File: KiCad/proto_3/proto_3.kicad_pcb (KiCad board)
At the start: 2 copper layers, 129 x 49 mm, 13 parts, among them J1 1729128, J2 1729128

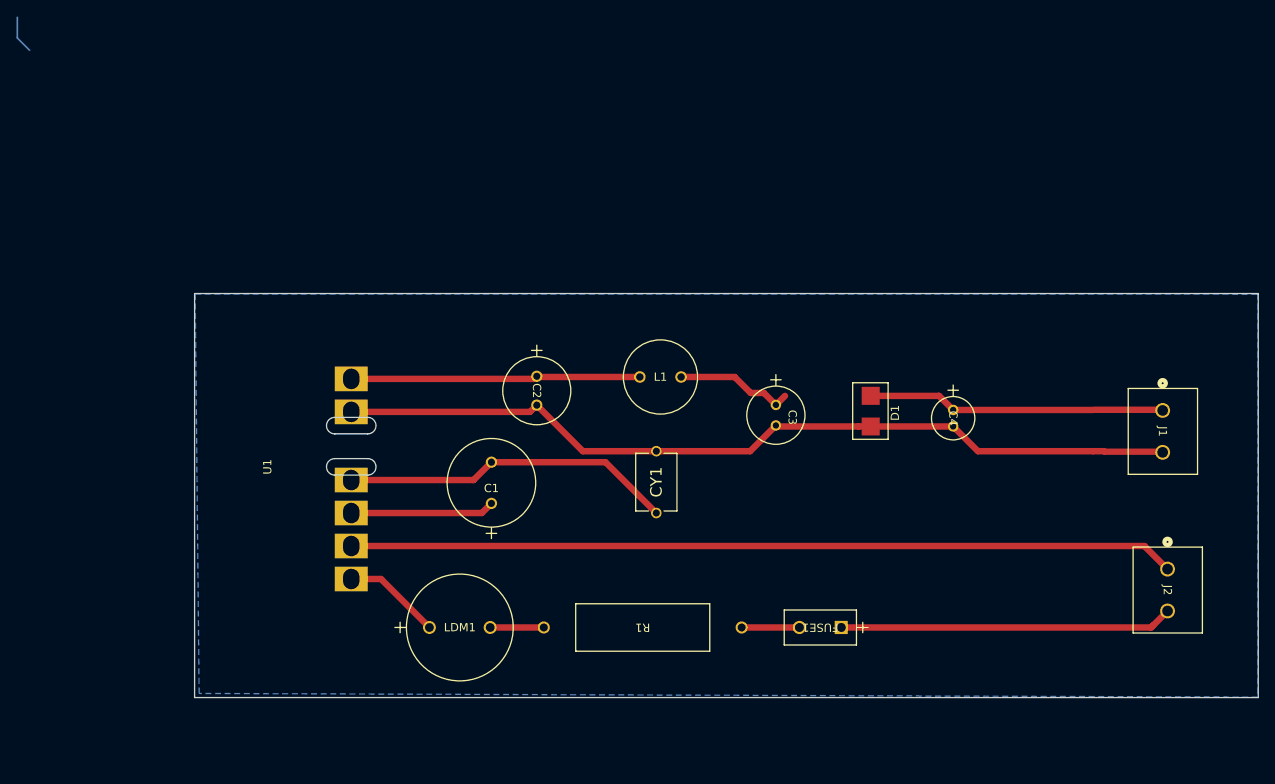
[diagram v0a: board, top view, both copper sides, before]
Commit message: changed space between traces on high voltage rail
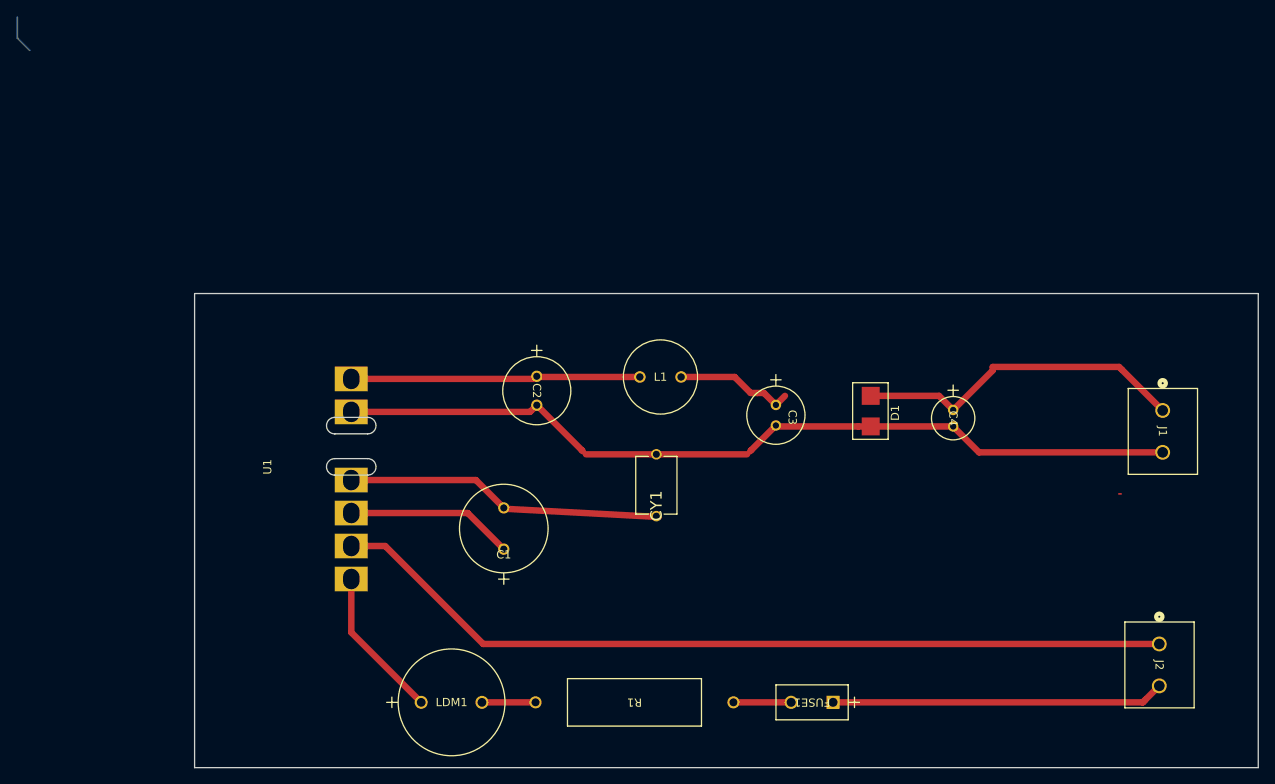
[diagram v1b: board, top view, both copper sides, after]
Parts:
- moved FUSE1 9.13 mm to (174.9, 137.6)
- moved LDM1 9.13 mm to (125.0, 137.6)
- moved R1 9.13 mm to (162.8, 137.6)
- moved J2 9.13 mm to (214.5, 130.5)
- moved C1 5.75 mm to (135.0, 119.0)
- moved CY1 0.38 mm to (153.5, 111.2)
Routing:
- net /ACDC_VCAP_NEG: track 40.5 -> 19.9 mm
- net /AC_FILTER_OUT: track 11.9 -> 18.5 mm
- net /DC_OUT: track 52.2 -> 57.2 mm
- net /ACDC_VCAP_POS: track 17.5 -> 20.3 mm
- net /AC_IN_NEUTRAL: track 100.2 -> 102.9 mm
- net /GND: track 103.5 -> 104.6 mm
- removed copper zone on B.Cu, net /GND
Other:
- board size 129 x 49 mm -> 129 x 57.5 mm
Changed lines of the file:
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@@
 	(footprint "Resistor-300-3A:res2_1-1625892-1_TEC"
 		(layer "F.Cu")
-		(at 163.849749 128.5 180)
+		(at 162.849749 137.58 180)
 		(tags "ROX3SJ12R ")
 		(property "Reference" "R1"
@@
 	(footprint "stuff:AIUR-06_ABR"
 		(layer "F.Cu")
-		(at 125.98375 128.5)
+		(at 124.98375 137.58)
 		(tags "AIUR-06-472K ")
 		(property "Reference" "LDM1"
@@
 	(footprint "Capacitor-10uF-450V:CAP_BX_10x20_RUB"
 		(layer "F.Cu")
-		(at 133.5 113.45325 90)
+		(at 135 119 90)
 		(tags "450BXC10MEFC10X20 ")
 		(property "Reference" "C1"
-			(at 1.83325 0 0)
+			(at -0.66675 0 0)
 			(unlocked yes)
 			(layer "F.SilkS")
@@
 		)
 		(fp_text user "${REFERENCE}"
-			(at 1.83325 0 0)
+			(at -0.66675 0 0)
 			(unlocked yes)
 			(layer "F.Fab")
@@
 	(footprint "Capacitor-1nF-400V:CAP_DE2E3SA102MN3AY02F"
 		(layer "F.Cu")
-		(at 153.5 110.87 90)
+		(at 153.5 111.25 90)
 		(property "Reference" "CY1"
-			(at 0 0 90)
+			(at -2.5 0 90)
 			(layer "F.SilkS")
 			(effects
@@
 	(footprint "fuse_300V_1a:FUSE_36911_LTF"
 		(layer "F.Cu")
-		(at 175.92975 128.5 180)
+		(at 174.92975 137.58 180)
 		(tags "36911000000 ")
 		(property "Reference" "FUSE1"
@@
 	(footprint "stuff:CONN_1729128_PXC"
 		(layer "F.Cu")
-		(at 215.5 121.42 -90)
+		(at 214.5 130.5 -90)
 		(tags "1729128 ")
 		(property "Reference" "J2"
@@
 		(embedded_fonts no)
 	)
+	(gr_line
+		(start 135.1 114.1)
+		(end 153.8 115.1)
+		(stroke
+			(width 0.7814)
+			(type solid)
+		)
+		(layer "F.Cu")
+		(net 2)
+	)
 	(gr_rect
 		(start 97.5 88)
-		(end 226.5 137)
+		(end 226.5 145.5)
 		(stroke
 			(width 0.05)
@@
 	)
 	(segment
-		(start 132.33325 114.62)
-		(end 116.5 114.62)
+		(start 116.5 114.62)
+		(end 130.62 114.62)
 		(width 0.7814)
 		(layer "F.Cu")
@@
 	)
 	(segment
-		(start 133.5 113.45325)
-		(end 132.33325 114.62)
+		(start 130.62 114.62)
+		(end 135 119)
 		(width 0.7814)
 		(layer "F.Cu")
@@
 	)
 	(segment
-		(start 147.33325 108.45325)
-		(end 153.5 114.62)
+		(start 131.62 110.62)
+		(end 135 114)
 		(width 0.7814)
 		(layer "F.Cu")
@@
 	)
 	(segment
-		(start 133.5 108.45325)
-		(end 147.33325 108.45325)
+		(start 116.5 110.62)
+		(end 131.62 110.62)
 		(width 0.7814)
 		(layer "F.Cu")
@@
 	)
 	(segment
-		(start 133.5 108.45325)
-		(end 131.33325 110.62)
-		(width 0.7814)
-		(layer "F.Cu")
-		(net 2)
-	)
-	(segment
-		(start 131.33325 110.62)
-		(end 116.5 110.62)
-		(width 0.7814)
-		(layer "F.Cu")
-		(net 2)
-	)
-	(segment
-		(start 192.5 107.12)
-		(end 206.5 107.12)
+		(start 192.64 107.26)
+		(end 214.9092 107.26)
+		(width 0.7814)
+		(layer "F.Cu")
+		(net 3)
+	)
+	(segment
+		(start 144.463249 107)
+		(end 144.583249 107.12)
+		(width 0.7814)
+		(layer "F.Cu")
+		(net 3)
+	)
+	(segment
+		(start 189.5 104.12)
+		(end 192.64 107.26)
+		(width 0.7814)
+		(layer "F.Cu")
+		(net 3)
+	)
+	(segment
+		(start 153.5 107.5)
+		(end 164.5 107.5)
 		(width 0.7814)
 		(layer "F.Cu")
@@
 	)
 	(segment
+		(start 164.88 107.12)
+		(end 165 107)
+		(width 0.7814)
+		(layer "F.Cu")
+		(net 3)
+	)
+	(segment
 		(start 138.184751 102.352)
 		(end 139 101.536751)
@@
 	)
 	(segment
-		(start 139 101.536751)
-		(end 144.583249 107.12)
-		(width 0.7814)
+		(start 144.963249 107.5)
+		(end 144.463249 107)
+		(width 0.2)
 		(layer "F.Cu")
 		(net 3)
 	)
 	(segment
-		(start 153.5 107.12)
-		(end 164.88 107.12)
+		(start 153.5 107.5)
+		(end 144.963249 107.5)
 		(width 0.7814)
 		(layer "F.Cu")
@@
 	)
 	(segment
-		(start 206.5 107.12)
-		(end 207.8 107.12)
-		(width 0.7814)
+		(start 209.8692 112.3)
+		(end 209.6 112.3)
+		(width 0.2)
 		(layer "F.Cu")
 		(net 3)
 	)
 	(segment
-		(start 164.88 107.12)
+		(start 165 107)
 		(end 168 104)
 		(width 0.7814)
@@
 	)
 	(segment
-		(start 144.583249 107.12)
-		(end 153.5 107.12)
-		(width 0.7814)
-		(layer "F.Cu")
-		(net 3)
-	)
-	(segment
-		(start 207.860799 107.18)
-		(end 214.9092 107.18)
-		(width 0.7814)
-		(layer "F.Cu")
-		(net 3)
-	)
-	(segment
-		(start 189.5 104.12)
-		(end 192.5 107.12)
-		(width 0.7814)
+		(start 164.5 107.5)
+		(end 165 107)
+		(width 0.2)
 		(layer "F.Cu")
 		(net 3)
@@
 		(start 116.5 102.352)
 		(end 138.184751 102.352)
+		(width 0.7814)
+		(layer "F.Cu")
+		(net 3)
+	)
+	(segment
+		(start 139 101.536751)
+		(end 144.463249 107)
 		(width 0.7814)
 		(layer "F.Cu")
@@
 	)
 	(segment
+		(start 209.9646 97.2354)
+		(end 209.8 97.0708)
+		(width 0.2)
+		(layer "F.Cu")
+		(net 5)
+	)
+	(segment
 		(start 167.1092 100.62)
 		(end 168 101.5108)
@@
 	)
 	(segment
-		(start 206.640799 102.1)
-		(end 214.9092 102.1)
+		(start 194.3 96.9)
+		(end 209.6292 96.9)
+		(width 0.7814)
+		(layer "F.Cu")
+		(net 5)
+	)
+	(segment
+		(start 209.6292 96.9)
+		(end 209.9646 97.2354)
+		(width 0.7814)
+		(layer "F.Cu")
+		(net 5)
+	)
+	(segment
+		(start 189.5 102.12)
+		(end 194.3 97.32)
+		(width 0.7814)
+		(layer "F.Cu")
+		(net 5)
+	)
+	(segment
+		(start 209.9646 97.2354)
+		(end 214.9092 102.18)
 		(width 0.7814)
 		(layer "F.Cu")
@@
 	)
 	(segment
+		(start 194.3 97.32)
+		(end 194.3 96.9)
+		(width 0.7814)
+		(layer "F.Cu")
+		(net 5)
+	)
+	(segment
 		(start 187.79 100.41)
 		(end 179.5 100.41)
@@
 	)
 	(segment
-		(start 189.5 102.12)
-		(end 206.5 102.12)
-		(width 0.7814)
-		(layer "F.Cu")
-		(net 5)
-	)
-	(segment
 		(start 164.94 100.06)
 		(end 166.5492 100.06)
@@
 	)
 	(segment
-		(start 163.849751 128.5)
-		(end 170.84975 128.5)
+		(start 162.849751 137.58)
+		(end 169.84975 137.58)
 		(width 0.7814)
 		(layer "F.Cu")
@@
 	)
 	(segment
-		(start 213.5 128.5)
-		(end 215.5 126.5)
+		(start 212.5 137.58)
+		(end 214.5 135.58)
 		(width 0.7814)
 		(layer "F.Cu")
@@
 	)
 	(segment
-		(start 175.92975 128.5)
-		(end 213.5 128.5)
+		(start 174.92975 137.58)
+		(end 212.5 137.58)
 		(width 0.7814)
 		(layer "F.Cu")
@@
 	)
 	(segment
-		(start 213.5 128.5)
-		(end 213.8 128.2)
+		(start 212.5 137.58)
+		(end 212.8 137.28)
 		(width 0.7814)
 		(layer "F.Cu")
@@
 	)
 	(segment
-		(start 212.7 118.62)
-		(end 215.5 121.42)
+		(start 132.5 130.5)
+		(end 214.5 130.5)
 		(width 0.7814)
 		(layer "F.Cu")
@@
 	(segment
 		(start 116.5 118.62)
-		(end 212.7 118.62)
+		(end 120.62 118.62)
 		(width 0.7814)
 		(layer "F.Cu")
@@
 	)
 	(segment
-		(start 139.84975 128.5)
-		(end 133.34975 128.5)
+		(start 120.62 118.62)
+		(end 132.5 130.5)
+		(width 0.7814)
+		(layer "F.Cu")
+		(net 8)
+	)
+	(segment
+		(start 138.84975 137.58)
+		(end 132.34975 137.58)
 		(width 0.7814)
 		(layer "F.Cu")
@@
 	)
 	(segment
-		(start 120.10375 122.62)
-		(end 125.98375 128.5)
+		(start 116.5 122.62)
+		(end 116.5 129.09625)
 		(width 0.7814)
 		(layer "F.Cu")
@@
 	)
 	(segment
-		(start 116.5 122.62)
-		(end 120.10375 122.62)
+		(start 116.5 129.09625)
+		(end 124.98375 137.58)
 		(width 0.7814)
 		(layer "F.Cu")
 		(net 10)
 	)
-	(zone
-		(net 3)
-		(net_name "/GND")
-		(layer "B.Cu")
-		(hatch edge 0.5)
-		(connect_pads
-			(clearance 0.5)
-		)
-		(min_thickness 0.25)
-		(filled_areas_thickness no)
-		(fill yes
-			(thermal_gap 0.5)
-			(thermal_bridge_width 0.5)
-		)
-		(polygon
-			(pts
-				(xy 97.575 88.05) (xy 226.425 88.075) (xy 226.45 136.95) (xy 98.05 136.5)
-			)
-		)
-	)
 	(embedded_fonts no)

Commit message: added step files back to footprints, moved traces around
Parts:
- moved CY1 0.35 mm to (153.6, 110.9)
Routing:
- net /DC_OUT: track 57.2 -> 64.2 mm
- net /GND: track 104.6 -> 105.1 mm
- net /AC_IN_NEUTRAL: track 102.9 -> 103.4 mm
- added copper zone on B.Cu, net /GND
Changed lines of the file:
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@@
 		)
 		(embedded_fonts no)
+		(model "/home/none/Downloads/3d_models/UFW1C471MPD(1)/CAP_RHT_8X11P5_NCH.step"
+			(offset
+				(xyz 0 0 0)
+			)
+			(scale
+				(xyz 1 1 1)
+			)
+			(rotate
+				(xyz 0 0 0)
+			)
+		)
 	)
 	(footprint "stuff:IND_RLB9012-4R7ML"
@@
 		(embedded_fonts no)
 		(model "/home/none/Downloads/3d_models/UFW1H0R1MDD1TA(1)/CAP_UEP_5X11_NCH.step"
-			(hide yes)
 			(offset
 				(xyz 0 0 0)
@@
 	(footprint "Capacitor-1nF-400V:CAP_DE2E3SA102MN3AY02F"
 		(layer "F.Cu")
-		(at 153.5 111.25 90)
+		(at 153.55 110.9 90)
 		(property "Reference" "CY1"
-			(at -2.5 0 90)
+			(at 0 0 90)
 			(layer "F.SilkS")
 			(effects
@@
 		(embedded_fonts no)
 		(model "/home/none/Downloads/3d_models/35ZLJ100M6_3X11(1)/CAP_6_3X11_RUB.step"
-			(hide yes)
 			(offset
 				(xyz 0 0 0)
@@
 	)
 	(gr_line
-		(start 135.1 114.1)
-		(end 153.8 115.1)
+		(start 135 114)
+		(end 137 114.5)
+		(stroke
+			(width 0.7814)
+			(type solid)
+		)
+		(layer "F.Cu")
+		(net 2)
+	)
+	(gr_line
+		(start 137 114.5)
+		(end 153.55 114.65)
 		(stroke
 			(width 0.7814)
@@
 	)
 	(segment
-		(start 192.64 107.26)
-		(end 214.9092 107.26)
+		(start 189.6 104.1)
+		(end 189.9354 104.1)
 		(width 0.7814)
 		(layer "F.Cu")
@@
 	)
 	(segment
-		(start 189.5 104.12)
-		(end 192.64 107.26)
+		(start 153.5 107.2)
+		(end 164.5 107.2)
 		(width 0.7814)
 		(layer "F.Cu")
@@
 	)
 	(segment
-		(start 153.5 107.5)
-		(end 164.5 107.5)
+		(start 168 104.12)
+		(end 178 104.12)
 		(width 0.7814)
 		(layer "F.Cu")
@@
 	)
 	(segment
-		(start 168 104.12)
-		(end 178 104.12)
+		(start 193 107.5)
+		(end 214.6692 107.5)
 		(width 0.7814)
 		(layer "F.Cu")
@@
 	)
 	(segment
-		(start 153.5 107.5)
-		(end 144.963249 107.5)
+		(start 153.468375 107.2)
+		(end 144.931624 107.2)
 		(width 0.7814)
 		(layer "F.Cu")
@@
 	)
 	(segment
+		(start 189.5277 104.0277)
+		(end 193 107.5)
+		(width 0.7814)
+		(layer "F.Cu")
+		(net 3)
+	)
+	(segment
+		(start 214.6692 107.5)
+		(end 214.9092 107.26)
+		(width 0.7814)
+		(layer "F.Cu")
+		(net 3)
+	)
+	(segment
 		(start 116.5 102.352)
 		(end 138.184751 102.352)
@@
 	)
 	(segment
-		(start 156.5 98.12)
-		(end 163 98.12)
+		(start 189.5154 102.18)
+		(end 203.5 102.18)
 		(width 0.7814)
 		(layer "F.Cu")
@@
 	)
 	(segment
-		(start 179.29 100.62)
-		(end 179.5 100.41)
-		(width 0.2)
-		(layer "F.Cu")
-		(net 5)
-	)
-	(segment
-		(start 209.9646 97.2354)
-		(end 209.8 97.0708)
-		(width 0.2)
+		(start 156.5 98.12)
+		(end 163 98.12)
+		(width 0.7814)
 		(layer "F.Cu")
 		(net 5)
 	)
 	(segment
-		(start 167.1092 100.62)
-		(end 168 101.5108)
-		(width 0.2)
+		(start 169.1008 100.41)
+		(end 176.59 100.41)
+		(width 0.7814)
 		(layer "F.Cu")
 		(net 5)
 	)
 	(segment
-		(start 163 98.12)
-		(end 164.94 100.06)
+		(start 203.5 102.18)
+		(end 204.4846 102.18)
 		(width 0.7814)
 		(layer "F.Cu")
@@
 	)
 	(segment
-		(start 194.3 96.9)
-		(end 209.6292 96.9)
-		(width 0.7814)
+		(start 179.29 100.62)
+		(end 179.5 100.41)
+		(width 0.2)
 		(layer "F.Cu")
 		(net 5)
 	)
 	(segment
-		(start 209.6292 96.9)
-		(end 209.9646 97.2354)
-		(width 0.7814)
+		(start 209.9646 97.2354)
+		(end 209.8 97.0708)
+		(width 0.2)
 		(layer "F.Cu")
 		(net 5)
 	)
 	(segment
-		(start 189.5 102.12)
-		(end 194.3 97.32)
-		(width 0.7814)
+		(start 167.1092 100.62)
+		(end 168 101.5108)
+		(width 0.2)
 		(layer "F.Cu")
 		(net 5)
 	)
 	(segment
-		(start 209.9646 97.2354)
-		(end 214.9092 102.18)
+		(start 163 98.12)
+		(end 164.94 100.06)
 		(width 0.7814)
 		(layer "F.Cu")
@@
 	)
 	(segment
-		(start 194.3 97.32)
-		(end 194.3 96.9)
+		(start 203.5 102.18)
+		(end 214.9092 102.18)
+		(width 0.7814)
+		(layer "F.Cu")
+		(net 5)
+	)
+	(segment
+		(start 189.3354 102)
+		(end 189.5154 102.18)
 		(width 0.7814)
 		(layer "F.Cu")
@@
 	)
 	(segment
+		(start 176.59 100.41)
+		(end 179.5 100.41)
+		(width 0.7814)
+		(layer "F.Cu")
+		(net 5)
+	)
+	(segment
 		(start 164.94 100.06)
 		(end 166.5492 100.06)
@@
 	)
 	(segment
-		(start 132.5 130.5)
-		(end 214.5 130.5)
+		(start 130.5 128.5)
+		(end 212.5 128.5)
+		(width 0.7814)
+		(layer "F.Cu")
+		(net 8)
+	)
+	(segment
+		(start 214.5 130.5)
+		(end 212.5 128.5)
 		(width 0.7814)
 		(layer "F.Cu")
@@
 	)
 	(segment
+		(start 130.5 128.5)
+		(end 131 128.5)
+		(width 0.7814)
+		(layer "F.Cu")
+		(net 8)
+	)
+	(segment
 		(start 120.62 118.62)
-		(end 132.5 130.5)
+		(end 130.5 128.5)
 		(width 0.7814)
 		(layer "F.Cu")
@@
 		(net 10)
 	)
+	(zone
+		(net 3)
+		(net_name "/GND")
+		(layer "B.Cu")
+		(hatch edge 0.5)
+		(connect_pads
+			(clearance 0.5)
+		)
+		(min_thickness 0.25)
+		(filled_areas_thickness no)
+		(fill yes
+			(thermal_gap 0.5)
+			(thermal_bridge_width 0.5)
+		)
+		(polygon
+			(pts
+				(xy 97.7 88.1) (xy 226.5 88) (xy 226.5 145.5) (xy 97.5 145.5) (xy 97.5 88.1) (xy 98.15 88.1)
+			)
+		)
+	)
 	(embedded_fonts no)
